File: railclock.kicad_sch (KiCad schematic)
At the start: 176 parts, among them J1 Conn_01x02_Pin, J10 Conn_01x04_MountingPin, J11 Conn_01x04_MountingPin, J12 Conn_01x04_MountingPin, J13 Conn_01x04_MountingPin, J14 Conn_01x04_MountingPin, J15 Conn_01x03_MountingPin, J16 Barrel_Jack_Switch, J3 Conn_01x04_MountingPin, J4 USB_C_Receptacle_USB2.0_14P, J5 Conn_01x03_MountingPin, J6 Conn_01x03_MountingPin, J7 Conn_01x03_MountingPin, J8 Conn_01x03_MountingPin, J9 Conn_01x04_MountingPin, K1 G6K-2, K2 G6K-2, K3 G6K-2, K4 G6K-2, K6 G6K-2, Q1 NPN, Q2 NPN, Q3 NPN, Q4 NPN, Q5 NPN, SW1 SW_SPST, SW2 SW_DPDT_x2, U1 MCP7940N-xST, U11 MAX811TEUS-T, U12 MCP4728, U2 MCP73832-2-OT, U4 ESP32-C6-WROOM-1, U5 DRV8870DDA, U6 PAM2421, U8 BQ24296MRGET, U9 PCF8574RGTR, Y2 Crystal_GND3

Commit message: Fix issues with first version
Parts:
- removed D3, D4, D5, D7, D8: D, Diode_SMD:D_MiniMELF, symbol Device:D
- removed K1, K2, K3, K4, K6: G6K-2, Relay_SMD:Relay_DPDT_Omron_G6K-2F-Y, symbol Relay:G6K-2
- removed Q1, Q2, Q3, Q4, Q5: NPN, Package_TO_SOT_SMD:SOT-23, symbol Simulation_SPICE:NPN
- removed R54, R55, R56, R57, R58, R59, R60, R61, R62, R63, R64, R77, R78, R79, R80, R81: R, Resistor_SMD:R_0805_2012Metric, symbol Device:R
- added C32, C33, C34, C35, C36, C37: C, Capacitor_SMD:C_0805_2012Metric, symbol Device:C
- added J2: Conn_01x03_MountingPin, Connector_JST:JST_PH_S3B-PH-SM4-TB_1x03-1MP_P2.00mm_Horizontal, symbol Connector_Generic_MountingPin:Conn_01x03_MountingPin
- added R22: R, Resistor_SMD:R_0805_2012Metric, symbol Device:R
- added U10: 74AHC1G04, Package_TO_SOT_SMD:SOT-23-5, symbol 74xGxx:74AHC1G04
- added U13, U14, U15, U16, U17: BTS5012SDA, Package_TO_SOT_SMD:TO-252-4, symbol Power_Management:BTS5012SDA
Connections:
- net +12V: now also J10.2 (Pin_2), J11.2 (Pin_2), J12.2 (Pin_2), J13.2 (Pin_2), J14.2 (Pin_2), C33.1, C34.1, C35.1, C36.1, C37.1, U13.3 (Vbb), U14.3 (Vbb), U15.3 (Vbb), U16.3 (Vbb), U17.3 (Vbb); no longer J10.3 (Pin_3), J11.3 (Pin_3), J12.3 (Pin_3), J13.3 (Pin_3), J14.3 (Pin_3)
- net +3.3V: now also J10.3 (Pin_3), J11.3 (Pin_3), J12.3 (Pin_3), J13.3 (Pin_3), J14.3 (Pin_3), C32.1, J2.2 (Pin_2), U10.5 (VCC); no longer R47.1, R51.1, R53.1
- net BOOT1: now also J2.1 (Pin_1)
- net GND: now also R47.2, R49.2, R51.2, R53.2, C32.2, C33.2, C34.2, C35.2, C36.2, C37.2, J2.3 (Pin_3), J2.MP (MountPin), R22.2, U10.3 (GND); no longer R49.1
- net MOTOR_OUT1: no longer R50.1
- net MOTOR_OUT2: no longer R48.1
- net OUT0: now also U13.2 (IN); no longer R45.2
- net OUT1: now also R45.1, U14.2 (IN); no longer R52.1
- net OUT2: now also R48.1, U15.2 (IN)
- net OUT3: now also R50.1, U16.2 (IN)
- net OUT4: now also R52.1, U17.2 (IN)
- net VBUS_ENABLE: now also U10.2; no longer U3.1 (~{EN})
- net at J11.1 (Pin_1), R46.2: now also U13.1 (OUT), U13.5 (OUT)
- net at R50.2: now also J13.1 (Pin_1), U16.1 (OUT), U16.5 (OUT); no longer R51.2
- net at R48.2: now also J12.1 (Pin_1), U15.1 (OUT), U15.5 (OUT); no longer R49.2
- net at J14.1 (Pin_1): now also R52.2, U17.1 (OUT), U17.5 (OUT)
- net at J10.1 (Pin_1): now also R45.2, U14.1 (OUT), U14.5 (OUT); no longer R52.2
- new net: R53.1, U17.4 (IS)
- new net: R22.1, U13.4 (IS)
- new net: R51.1, U16.4 (IS)
- new net: U10.4, U3.1 (~{EN})
- new net: R47.1, U14.4 (IS)
- new net: R49.1, U15.4 (IS)
- no-connect marks 14 -> 4

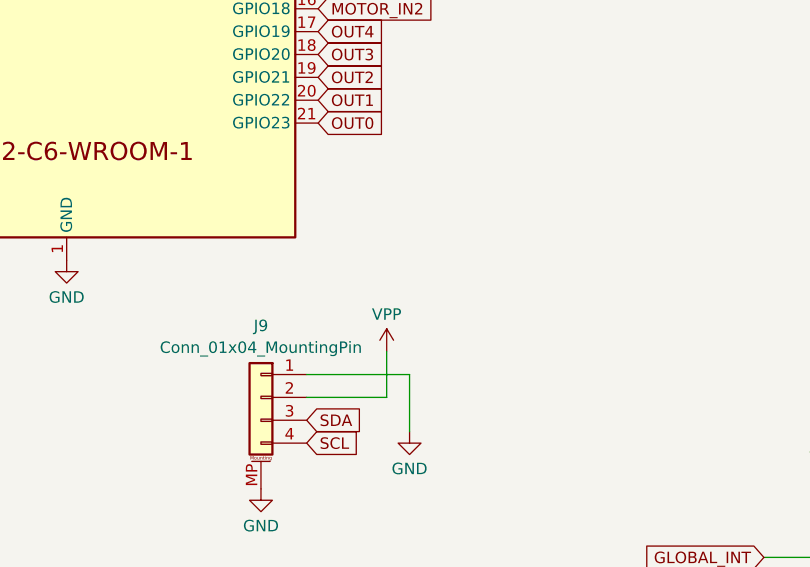
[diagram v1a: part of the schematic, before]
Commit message: Add option to choose which volatage is avaialble on the I2C connector
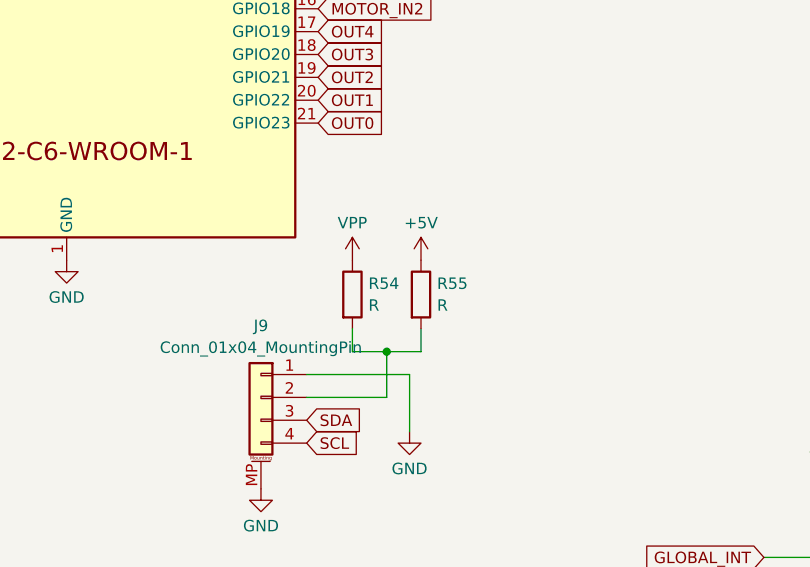
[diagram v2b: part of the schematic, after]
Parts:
- added R54, R55: R, Resistor_SMD:R_0805_2012Metric, symbol Device:R
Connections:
- net +5V: now also R55.1
- net VPP: now also R54.1; no longer J9.2 (Pin_2)
- new net: J9.2 (Pin_2), R54.2, R55.2

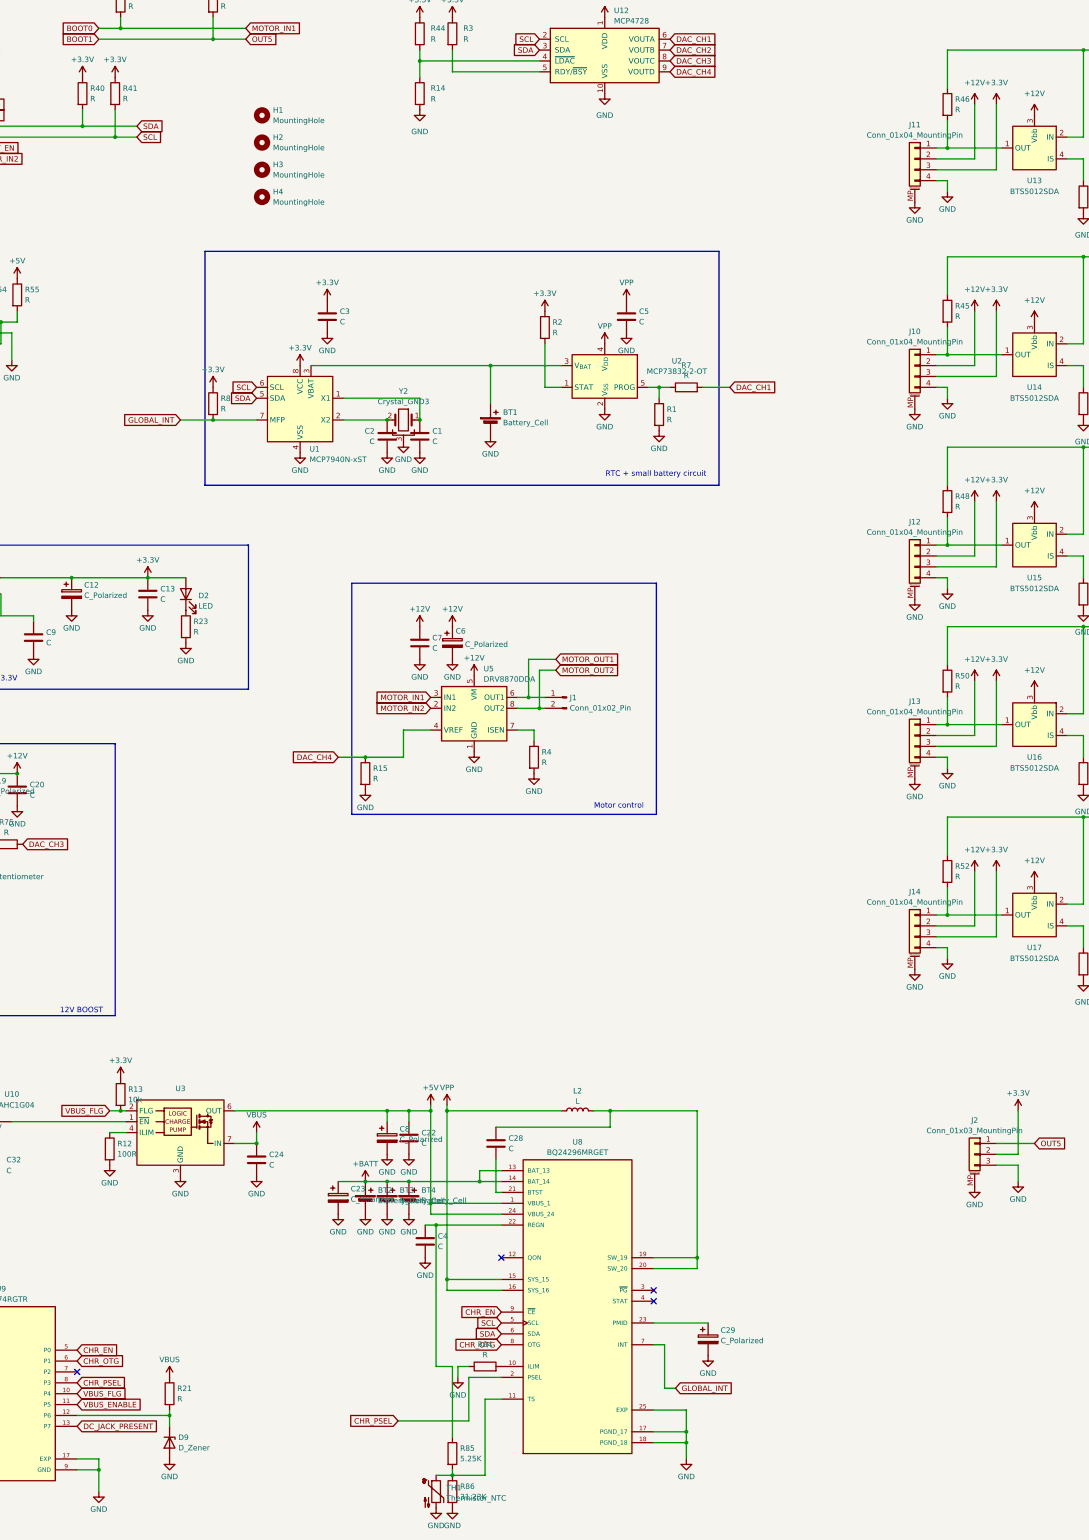
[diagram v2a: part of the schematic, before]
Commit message: Update board, rewire digital connections
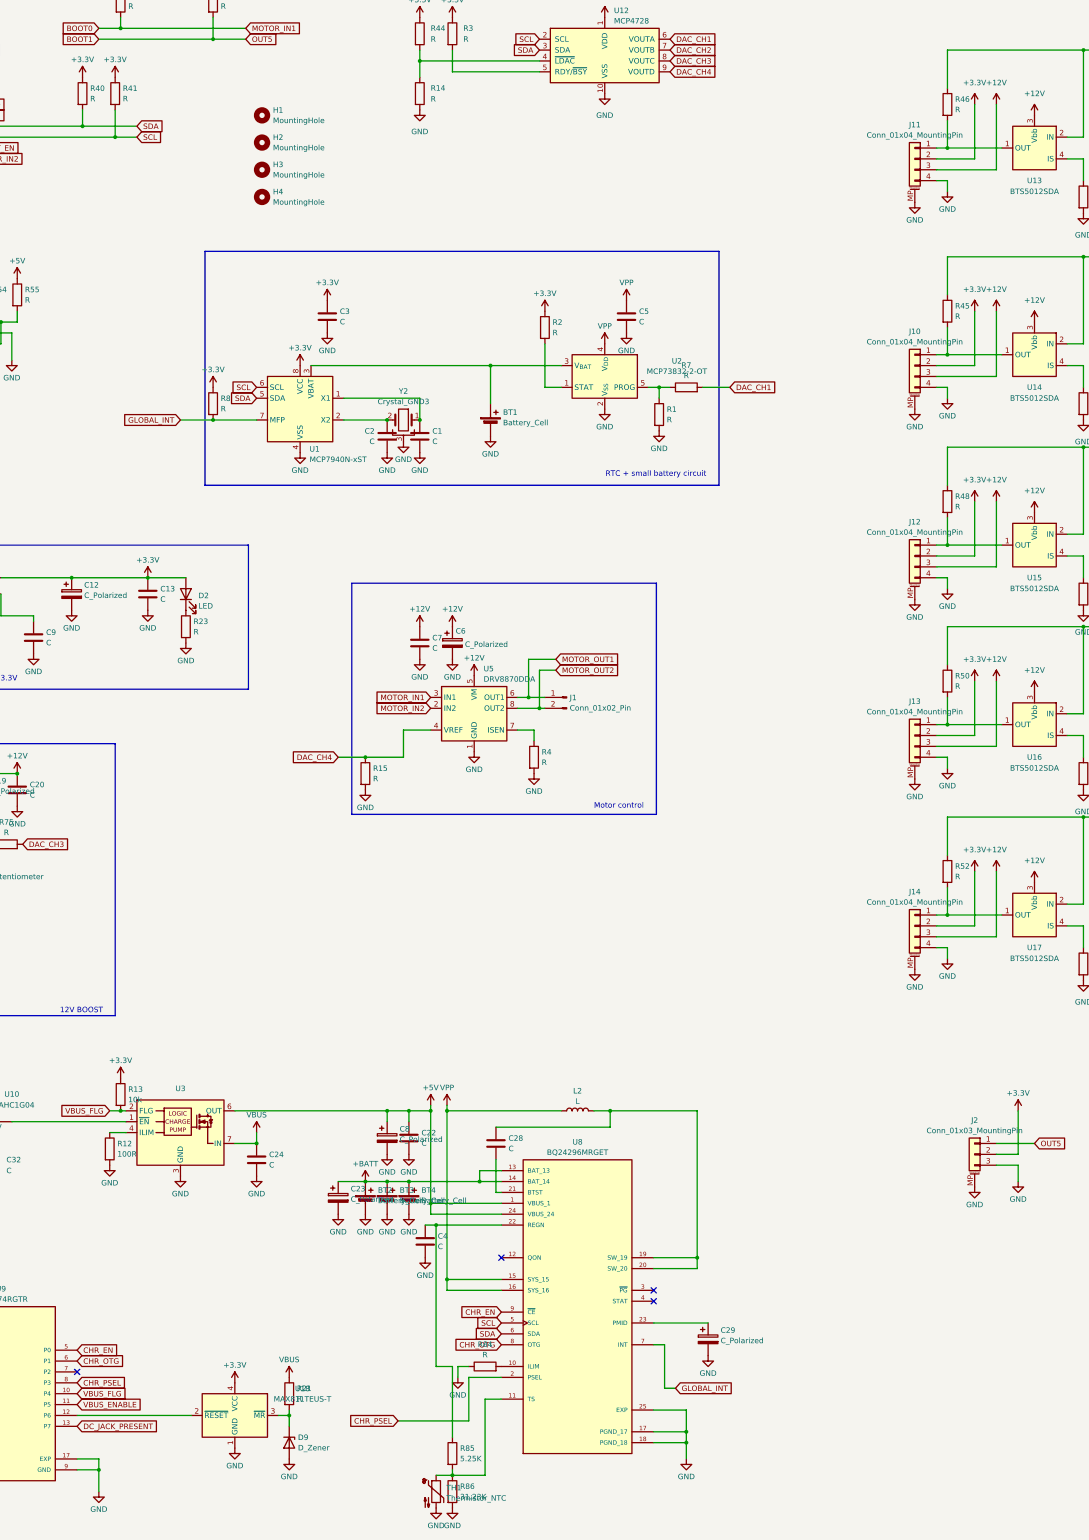
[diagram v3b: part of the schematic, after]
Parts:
- added U18: MAX811TEUS-T, Package_TO_SOT_SMD:SOT-143, symbol Power_Supervisor:MAX811TEUS-T
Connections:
- net +12V: now also J10.3 (Pin_3), J11.3 (Pin_3), J12.3 (Pin_3), J13.3 (Pin_3), J14.3 (Pin_3); no longer J10.2 (Pin_2), J11.2 (Pin_2), J12.2 (Pin_2), J13.2 (Pin_2), J14.2 (Pin_2)
- net +3.3V: now also J10.2 (Pin_2), J11.2 (Pin_2), J12.2 (Pin_2), J13.2 (Pin_2), J14.2 (Pin_2), U18.4 (VCC); no longer J10.3 (Pin_3), J11.3 (Pin_3), J12.3 (Pin_3), J13.3 (Pin_3), J14.3 (Pin_3)
- net GND: now also U18.1 (GND)
- net at D9.1 (K), R21.2: now also U18.3 (~{MR}); no longer U9.12 (P6)
- new net: U18.2 (~{RESET}), U9.12 (P6)
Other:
- moved on the sheet: D9, R21

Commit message: Add transils to A-D pins, fix vbus detection
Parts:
- removed U18: MAX811TEUS-T, Package_TO_SOT_SMD:SOT-143, symbol Power_Supervisor:MAX811TEUS-T
- added D10, D11, D12, D13, D14, D15, D3, D4, D5, D7, D8: D_Zener, symbol Device:D_Zener
- added Q1: Q_NPN_BEC, symbol Transistor_BJT:Q_NPN_BEC
- added R56: 100k, symbol Device:R
- added R57: R, symbol Device:R
- D9: footprint Diode_SMD:D_MiniMELF -> (none)
- R21: footprint Resistor_SMD:R_0805_2012Metric -> (none)
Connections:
- net +3.3V: now also R57.1; no longer U10.5 (VCC)
- net ADC1: now also D9.1 (K)
- net ADC2: now also D8.1 (K)
- net ADC3: now also D7.1 (K)
- net ADC4: now also D5.1 (K)
- net ADC5: now also D4.1 (K)
- net ADC6: now also D3.1 (K)
- net BOOT1: now also D10.1 (K)
- net DAC_CH4: now also R57.2
- net GND: now also D10.2 (A), D11.2 (A), D12.2 (A), D13.2 (A), D14.2 (A), D15.2 (A), D3.2 (A), D4.2 (A), D5.2 (A), D7.2 (A), D8.2 (A), Q1.2 (E)
- net IN: now also U10.5 (VCC), R56.1
- net VBUS_ENABLE: now also R56.2
- net at U9.12 (P6): now also Q1.3 (C)
- net at R21.2: now also Q1.1 (B); no longer D9.1 (K)
- net at J12.1 (Pin_1), R48.2, U15.1 (OUT)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: now also D13.1 (K)
- net at J13.1 (Pin_1), R50.2, U16.1 (OUT)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: now also D12.1 (K)
- net at J14.1 (Pin_1), R52.2, U17.1 (OUT)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: now also D11.1 (K)
- net at J10.1 (Pin_1), R45.2, U14.1 (OUT)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: now also D14.1 (K)
- net at J11.1 (Pin_1), R46.2, U13.1 (OUT)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: now also D15.1 (K)
